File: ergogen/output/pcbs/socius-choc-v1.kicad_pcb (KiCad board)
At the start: 2 copper layers, 117.6 x 96.6 mm, 113 parts

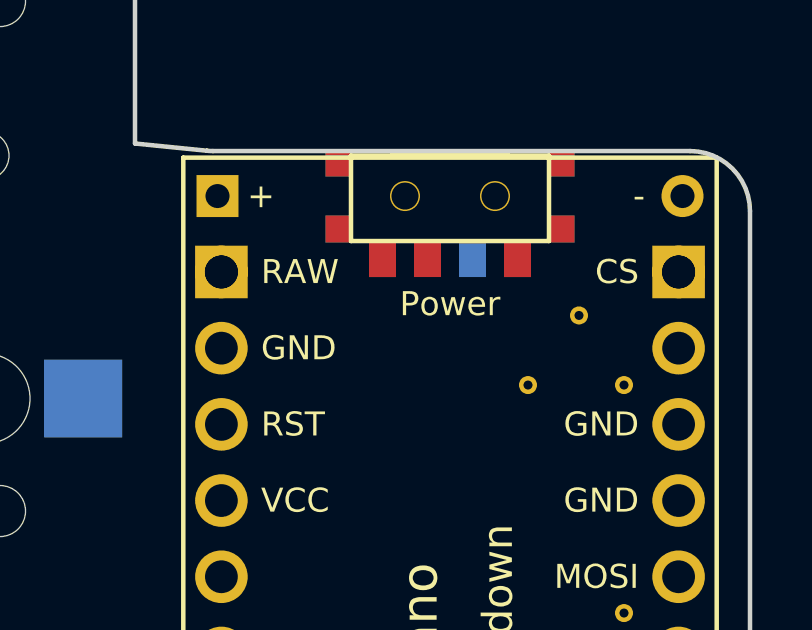
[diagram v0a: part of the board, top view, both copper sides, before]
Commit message: adding reversable mcu
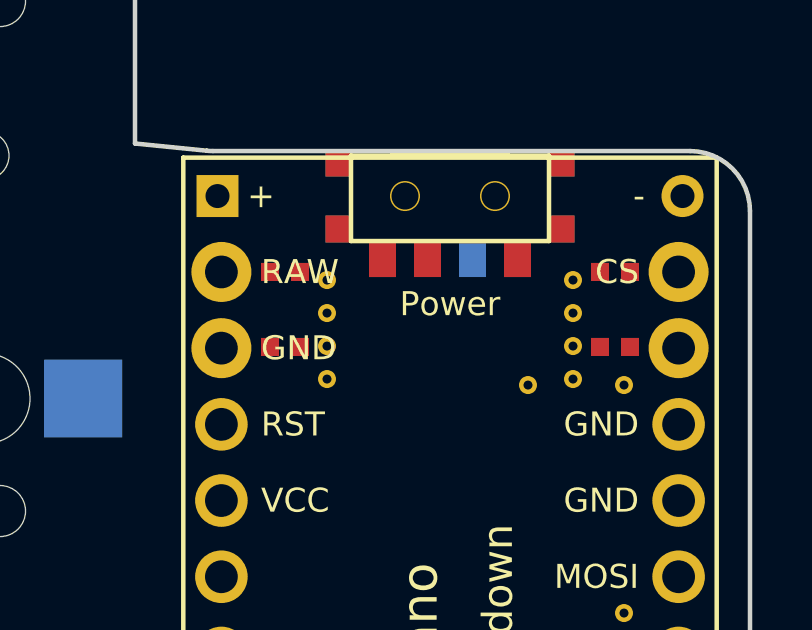
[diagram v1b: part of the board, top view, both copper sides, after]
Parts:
- removed the REF** at (256.9, 125.1)
- added REF**: VIA-0.6mm, VIA-0.6mm, F.Cu at (248.5, 124.0)
- added REF**: VIA-0.6mm, VIA-0.6mm, F.Cu at (256.7, 124.0)
- added REF**: VIA-0.6mm, VIA-0.6mm, F.Cu at (248.5, 125.1)
- added REF**: VIA-0.6mm, VIA-0.6mm, F.Cu at (256.7, 125.1)
- added REF**: VIA-0.6mm, VIA-0.6mm, F.Cu at (248.5, 126.2)
- added REF**: VIA-0.6mm, VIA-0.6mm, F.Cu at (256.7, 126.2)
- added REF**: VIA-0.6mm, VIA-0.6mm, F.Cu at (248.5, 127.3)
- added REF**: VIA-0.6mm, VIA-0.6mm, F.Cu at (256.7, 127.3)
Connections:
- MCU1 pad : CS -> P0
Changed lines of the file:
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@@
           (fp_text user "Place face Up" (at -4.7 -1.6 -90) (layer B.SilkS) (effects (font (size 1.0 1.0) (thickness 0.15)) (justify left mirror)))
           (fp_text user "SOCIUS v0.1" (at 17 0 0) (layer F.SilkS knockout) (effects (font (size 1.2 1.2) (thickness 0.20))))
-          (pad 1 thru_hole circle (at -13.97 7.62 -90) (size 1.7526 1.7526) (drill 1.0922) (layers *.Cu *.SilkS *.Mask) (net 27 "RAW"))
-          (pad 2 thru_hole circle (at -11.43 7.62 0) (size 1.7526 1.7526) (drill 1.0922) (layers *.Cu *.SilkS *.Mask) (net 28 "GND"))
+          (pad 1 thru_hole circle (at -13.97 7.62 -90) (size 2 2) (drill 1.0922) (layers F.Cu F.SilkS F.Mask) (net 27 "RAW"))
+          (pad 13 thru_hole circle (at -13.97 7.62 -90) (size 2 2) (drill 1.0922) (layers B.Cu B.SilkS B.Mask) (net 34 "CS"))
+          (pad 2 thru_hole circle (at -11.43 7.62 0) (size 2 2) (drill 1.0922) (layers F.Cu F.SilkS F.Mask) (net 28 "GND"))
+          (pad 14 thru_hole circle (at -11.43 7.62 0) (size 2 2) (drill 1.0922) (layers B.Cu B.SilkS B.Mask) (net 35 "P0"))
           (pad 3 thru_hole circle (at -8.89 7.62 0) (size 1.7526 1.7526) (drill 1.0922) (layers *.Cu *.SilkS *.Mask) (net 29 "RST"))
           (pad 4 thru_hole circle (at -6.35 7.62 0) (size 1.7526 1.7526) (drill 1.0922) (layers *.Cu *.SilkS *.Mask) (net 30 "VCC"))
@@
           (pad 11 thru_hole circle (at 11.43 7.62 0) (size 1.7526 1.7526) (drill 1.0922) (layers *.Cu *.SilkS *.Mask) (net 13 "COL3"))
           (pad 12 thru_hole circle (at 13.97 7.62 0) (size 1.7526 1.7526) (drill 1.0922) (layers *.Cu *.SilkS *.Mask) (net 17 "COL4"))
-          (pad 13 thru_hole circle (at -13.97 -7.62 0) (size 1.7526 1.7526) (drill 1.0922) (layers *.Cu *.SilkS *.Mask) (net 34 "CS"))
-          (pad 14 thru_hole circle (at -11.43 -7.62 0) (size 1.7526 1.7526) (drill 1.0922) (layers *.Cu *.SilkS *.Mask) (net 35 "P0"))
+          (pad 13 thru_hole circle (at -13.97 -7.62 0) (size 2 2) (drill 1.0922) (layers F.Cu F.SilkS F.Mask) (net 34 "CS"))
+          (pad 1 thru_hole circle (at -13.97 -7.62 0) (size 2 2) (drill 1.0922) (layers B.Cu B.SilkS B.Mask) (net 27 "RAW"))
+          (pad 14 thru_hole circle (at -11.43 -7.62 0) (size 2 2) (drill 1.0922) (layers F.Cu F.SilkS F.Mask) (net 35 "P0"))
+          (pad 2 thru_hole circle (at -11.43 -7.62 0) (size 2 2) (drill 1.0922) (layers B.Cu B.SilkS B.Mask) (net 28 "GND"))
           (pad 15 thru_hole circle (at -8.89 -7.62 0) (size 1.7526 1.7526) (drill 1.0922) (layers *.Cu *.SilkS *.Mask) (net 28 "GND"))
           (pad 16 thru_hole circle (at -6.35 -7.62 0) (size 1.7526 1.7526) (drill 1.0922) (layers *.Cu *.SilkS *.Mask) (net 28 "GND"))
@@
           (pad 23 thru_hole circle (at 11.43 -7.62 0) (size 1.7526 1.7526) (drill 1.0922) (layers *.Cu *.SilkS *.Mask) (net 23 "ROW2"))
           (pad 24 thru_hole circle (at 13.97 -7.62 0) (size 1.7526 1.7526) (drill 1.0922) (layers *.Cu *.SilkS *.Mask) (net 26 "ROW3"))
-          (pad "" thru_hole rect (at -13.97 7.62 -90) (size 1.7526 1.7526) (drill 1.1) (layers F.Cu F.Mask) (zone_connect 0) (net 27 "RAW"))
-          (pad "" thru_hole rect (at -13.97 -7.62 -90) (size 1.7526 1.7526) (drill 1.1) (layers B.Cu B.Mask) (zone_connect 0) (net 34 "CS"))
+          (pad "" connect rect (at -13.97 6 -90) (size 0.6 0.6) (layers F.Cu F.Mask) (zone_connect 0) (net 27 "RAW"))
+          (pad "" connect rect (at -13.97 5 -90) (size 0.6 0.6) (layers F.Cu F.Mask) (zone_connect 0) (net 27 "RAW"))
+          (pad "" connect rect (at -13.97 6 -90) (size 0.6 0.6) (layers B.Cu B.Mask) (zone_connect 0) (net 34 "CS"))
+          (pad "" connect rect (at -13.97 5 -90) (size 0.6 0.6) (layers B.Cu B.Mask) (zone_connect 0) (net 34 "CS"))
+          (pad "" connect rect (at -13.97 -6 -90) (size 0.6 0.6) (layers B.Cu B.Mask) (zone_connect 0) (net 27 "RAW"))
+          (pad "" connect rect (at -13.97 -5 -90) (size 0.6 0.6) (layers B.Cu B.Mask) (zone_connect 0) (net 27 "RAW"))
+          (pad "" connect rect (at -13.97 -6 -90) (size 0.6 0.6) (layers F.Cu F.Mask) (zone_connect 0) (net 34 "CS"))
+          (pad "" connect rect (at -13.97 -5 -90) (size 0.6 0.6) (layers F.Cu F.Mask) (zone_connect 0) (net 34 "CS"))
+          (pad "" connect rect (at -11.47 6 -90) (size 0.6 0.6) (layers F.Cu F.Mask) (zone_connect 0) (net 28 "GND"))
+          (pad "" connect rect (at -11.47 5 -90) (size 0.6 0.6) (layers F.Cu F.Mask) (zone_connect 0) (net 28 "GND"))
+          (pad "" connect rect (at -11.47 6 -90) (size 0.6 0.6) (layers B.Cu B.Mask) (zone_connect 0) (net 35 "P0"))
+          (pad "" connect rect (at -11.47 5 -90) (size 0.6 0.6) (layers B.Cu B.Mask) (zone_connect 0) (net 35 "P0"))
+          (pad "" connect rect (at -11.47 -6 -90) (size 0.6 0.6) (layers B.Cu B.Mask) (zone_connect 0) (net 28 "GND"))
+          (pad "" connect rect (at -11.47 -5 -90) (size 0.6 0.6) (layers B.Cu B.Mask) (zone_connect 0) (net 28 "GND"))
+          (pad "" connect rect (at -11.47 -6 -90) (size 0.6 0.6) (layers F.Cu F.Mask) (zone_connect 0) (net 35 "P0"))
+          (pad "" connect rect (at -11.47 -5 -90) (size 0.6 0.6) (layers F.Cu F.Mask) (zone_connect 0) (net 35 "P0"))
         )
         (module lib:niceview_headers (layer F.Cu)
@@
 		  )
       (module VIA-0.6mm (layer F.Cu)
+      (at 248.5447522 123.966967 0)
+      (fp_text reference REF** (at 0 1.4) (layer F.SilkS) hide (effects (font (size 1 1) (thickness 0.15))))
+      (fp_text value VIA-0.6mm (at 0 -1.4) (layer F.Fab) hide (effects (font (size 1 1) (thickness 0.15))))
+      (pad 1 thru_hole circle (at 0 0) (size 0.6 0.6) (drill 0.3) (layers *.Cu) (zone_connect 2) (net 27 "RAW"))
+      )
+      (module VIA-0.6mm (layer F.Cu)
+      (at 256.7447522 123.966967 0)
+      (fp_text reference REF** (at 0 1.4) (layer F.SilkS) hide (effects (font (size 1 1) (thickness 0.15))))
+      (fp_text value VIA-0.6mm (at 0 -1.4) (layer F.Fab) hide (effects (font (size 1 1) (thickness 0.15))))
+      (pad 1 thru_hole circle (at 0 0) (size 0.6 0.6) (drill 0.3) (layers *.Cu) (zone_connect 2) (net 27 "RAW"))
+      )
+      (module VIA-0.6mm (layer F.Cu)
+      (at 248.5447522 125.066967 0)
+      (fp_text reference REF** (at 0 1.4) (layer F.SilkS) hide (effects (font (size 1 1) (thickness 0.15))))
+      (fp_text value VIA-0.6mm (at 0 -1.4) (layer F.Fab) hide (effects (font (size 1 1) (thickness 0.15))))
+      (pad 1 thru_hole circle (at 0 0) (size 0.6 0.6) (drill 0.3) (layers *.Cu) (zone_connect 2) (net 34 "CS"))
+      )
+      (module VIA-0.6mm (layer F.Cu)
+      (at 256.7447522 125.066967 0)
+      (fp_text reference REF** (at 0 1.4) (layer F.SilkS) hide (effects (font (size 1 1) (thickness 0.15))))
+      (fp_text value VIA-0.6mm (at 0 -1.4) (layer F.Fab) hide (effects (font (size 1 1) (thickness 0.15))))
+      (pad 1 thru_hole circle (at 0 0) (size 0.6 0.6) (drill 0.3) (layers *.Cu) (zone_connect 2) (net 34 "CS"))
+      )
+      (module VIA-0.6mm (layer F.Cu)
+      (at 248.5447522 126.166967 0)
+      (fp_text reference REF** (at 0 1.4) (layer F.SilkS) hide (effects (font (size 1 1) (thickness 0.15))))
+      (fp_text value VIA-0.6mm (at 0 -1.4) (layer F.Fab) hide (effects (font (size 1 1) (thickness 0.15))))
+      (pad 1 thru_hole circle (at 0 0) (size 0.6 0.6) (drill 0.3) (layers *.Cu) (zone_connect 2) (net 28 "GND"))
+      )
+      (module VIA-0.6mm (layer F.Cu)
+      (at 256.7447522 126.166967 0)
+      (fp_text reference REF** (at 0 1.4) (layer F.SilkS) hide (effects (font (size 1 1) (thickness 0.15))))
+      (fp_text value VIA-0.6mm (at 0 -1.4) (layer F.Fab) hide (effects (font (size 1 1) (thickness 0.15))))
+      (pad 1 thru_hole circle (at 0 0) (size 0.6 0.6) (drill 0.3) (layers *.Cu) (zone_connect 2) (net 28 "GND"))
+      )
+      (module VIA-0.6mm (layer F.Cu)
+      (at 248.5447522 127.266967 0)
+      (fp_text reference REF** (at 0 1.4) (layer F.SilkS) hide (effects (font (size 1 1) (thickness 0.15))))
+      (fp_text value VIA-0.6mm (at 0 -1.4) (layer F.Fab) hide (effects (font (size 1 1) (thickness 0.15))))
+      (pad 1 thru_hole circle (at 0 0) (size 0.6 0.6) (drill 0.3) (layers *.Cu) (zone_connect 2) (net 35 "P0"))
+      )
+      (module VIA-0.6mm (layer F.Cu)
+      (at 256.7447522 127.266967 0)
+      (fp_text reference REF** (at 0 1.4) (layer F.SilkS) hide (effects (font (size 1 1) (thickness 0.15))))
+      (fp_text value VIA-0.6mm (at 0 -1.4) (layer F.Fab) hide (effects (font (size 1 1) (thickness 0.15))))
+      (pad 1 thru_hole circle (at 0 0) (size 0.6 0.6) (drill 0.3) (layers *.Cu) (zone_connect 2) (net 35 "P0"))
+      )
+      (module VIA-0.6mm (layer F.Cu)
       (at 258.4447522 127.466967 0)
       (fp_text reference REF** (at 0 1.4) (layer F.SilkS) hide (effects (font (size 1 1) (thickness 0.15))))
@@
       )
       (module VIA-0.6mm (layer F.Cu)
-      (at 256.9447522 125.146967 0)
-      (fp_text reference REF** (at 0 1.4) (layer F.SilkS) hide (effects (font (size 1 1) (thickness 0.15))))
-      (fp_text value VIA-0.6mm (at 0 -1.4) (layer F.Fab) hide (effects (font (size 1 1) (thickness 0.15))))
-      (pad 1 thru_hole circle (at 0 0) (size 0.6 0.6) (drill 0.3) (layers *.Cu) (zone_connect 2) (net 25 "ROW0"))
-      )
-      (module VIA-0.6mm (layer F.Cu)

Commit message: routing reversable mcu
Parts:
- removed the REF** at (248.5, 124.0)
- removed the REF** at (256.7, 124.0)
- removed the REF** at (248.5, 125.1)
- removed the REF** at (256.7, 125.1)
- removed the REF** at (248.5, 126.2)
- removed the REF** at (256.7, 126.2)
- removed the REF** at (248.5, 127.3)
- removed the REF** at (256.7, 127.3)
- removed the REF** at (258.4, 127.5)
- removed the REF** at (255.2, 127.5)
- removed the REF** at (256.9, 144.0)
- removed the REF** at (258.4, 135.1)
- removed the REF** at (246.2, 159.7)
- removed the REF** at (258.4, 159.7)
- added REF**: VIA-0.6mm, VIA-0.6mm, F.Cu at (256.4, 142.5)
- added REF**: VIA-0.6mm, VIA-0.6mm, F.Cu at (248.8, 144.0)
- added REF**: VIA-0.6mm, VIA-0.6mm, F.Cu at (256.4, 144.0)
- added REF**: VIA-0.6mm, VIA-0.6mm, F.Cu at (248.8, 145.0)
- added REF**: VIA-0.6mm, VIA-0.6mm, F.Cu at (256.4, 145.0)
- added REF**: VIA-0.6mm, VIA-0.6mm, F.Cu at (248.8, 146.5)
- added REF**: VIA-0.6mm, VIA-0.6mm, F.Cu at (256.4, 146.5)
- added REF**: VIA-0.6mm, VIA-0.6mm, F.Cu at (248.8, 147.6)
- added REF**: VIA-0.6mm, VIA-0.6mm, F.Cu at (256.4, 147.6)
- added REF**: VIA-0.6mm, VIA-0.6mm, F.Cu at (248.8, 149.1)
- added REF**: VIA-0.6mm, VIA-0.6mm, F.Cu at (256.4, 149.1)
- added REF**: VIA-0.6mm, VIA-0.6mm, F.Cu at (248.8, 150.1)
- added REF**: VIA-0.6mm, VIA-0.6mm, F.Cu at (256.4, 150.1)
- added REF**: VIA-0.6mm, VIA-0.6mm, F.Cu at (248.8, 151.6)
- added REF**: VIA-0.6mm, VIA-0.6mm, F.Cu at (256.4, 151.6)
- added REF**: VIA-0.6mm, VIA-0.6mm, F.Cu at (248.8, 152.7)
- added REF**: VIA-0.6mm, VIA-0.6mm, F.Cu at (256.4, 152.7)
- added REF**: VIA-0.6mm, VIA-0.6mm, F.Cu at (249.2, 159.7)
- added REF**: VIA-0.6mm, VIA-0.6mm, F.Cu at (256.0, 159.7)
- added REF**: VIA-0.6mm, VIA-0.6mm, F.Cu at (248.8, 124.0)
- added REF**: VIA-0.6mm, VIA-0.6mm, F.Cu at (256.4, 124.0)
- added REF**: VIA-0.6mm, VIA-0.6mm, F.Cu at (248.8, 125.0)
- added REF**: VIA-0.6mm, VIA-0.6mm, F.Cu at (256.4, 125.0)
- added REF**: VIA-0.6mm, VIA-0.6mm, F.Cu at (248.8, 126.2)
- added REF**: VIA-0.6mm, VIA-0.6mm, F.Cu at (256.4, 126.2)
- added REF**: VIA-0.6mm, VIA-0.6mm, F.Cu at (248.8, 127.3)
- added REF**: VIA-0.6mm, VIA-0.6mm, F.Cu at (256.4, 127.3)
- added REF**: VIA-0.6mm, VIA-0.6mm, F.Cu at (248.8, 128.8)
- added REF**: VIA-0.6mm, VIA-0.6mm, F.Cu at (256.4, 128.8)
- added REF**: VIA-0.6mm, VIA-0.6mm, F.Cu at (248.8, 129.8)
- added REF**: VIA-0.6mm, VIA-0.6mm, F.Cu at (256.4, 129.8)
- added REF**: VIA-0.6mm, VIA-0.6mm, F.Cu at (248.8, 131.3)
- added REF**: VIA-0.6mm, VIA-0.6mm, F.Cu at (256.4, 131.3)
- added REF**: VIA-0.6mm, VIA-0.6mm, F.Cu at (248.8, 132.3)
- added REF**: VIA-0.6mm, VIA-0.6mm, F.Cu at (256.4, 132.3)
- added REF**: VIA-0.6mm, VIA-0.6mm, F.Cu at (248.8, 133.8)
- added REF**: VIA-0.6mm, VIA-0.6mm, F.Cu at (256.4, 133.8)
- added REF**: VIA-0.6mm, VIA-0.6mm, F.Cu at (248.8, 134.9)
- added REF**: VIA-0.6mm, VIA-0.6mm, F.Cu at (256.4, 134.9)
- added REF**: VIA-0.6mm, VIA-0.6mm, F.Cu at (248.8, 136.4)
- added REF**: VIA-0.6mm, VIA-0.6mm, F.Cu at (256.4, 136.4)
- added REF**: VIA-0.6mm, VIA-0.6mm, F.Cu at (248.8, 137.4)
- added REF**: VIA-0.6mm, VIA-0.6mm, F.Cu at (256.4, 137.4)
- added REF**: VIA-0.6mm, VIA-0.6mm, F.Cu at (248.8, 138.9)
- added REF**: VIA-0.6mm, VIA-0.6mm, F.Cu at (256.4, 138.9)
- added REF**: VIA-0.6mm, VIA-0.6mm, F.Cu at (248.8, 140.0)
- added REF**: VIA-0.6mm, VIA-0.6mm, F.Cu at (256.4, 140.0)
- added REF**: VIA-0.6mm, VIA-0.6mm, F.Cu at (248.8, 141.5)
- added REF**: VIA-0.6mm, VIA-0.6mm, F.Cu at (256.4, 141.5)
- added REF**: VIA-0.6mm, VIA-0.6mm, F.Cu at (248.8, 142.5)
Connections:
- MCU1 pad : P0 -> ROW3
